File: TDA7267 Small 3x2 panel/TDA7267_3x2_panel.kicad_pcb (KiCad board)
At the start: 2 copper layers, 89 x 99 mm, 108 parts

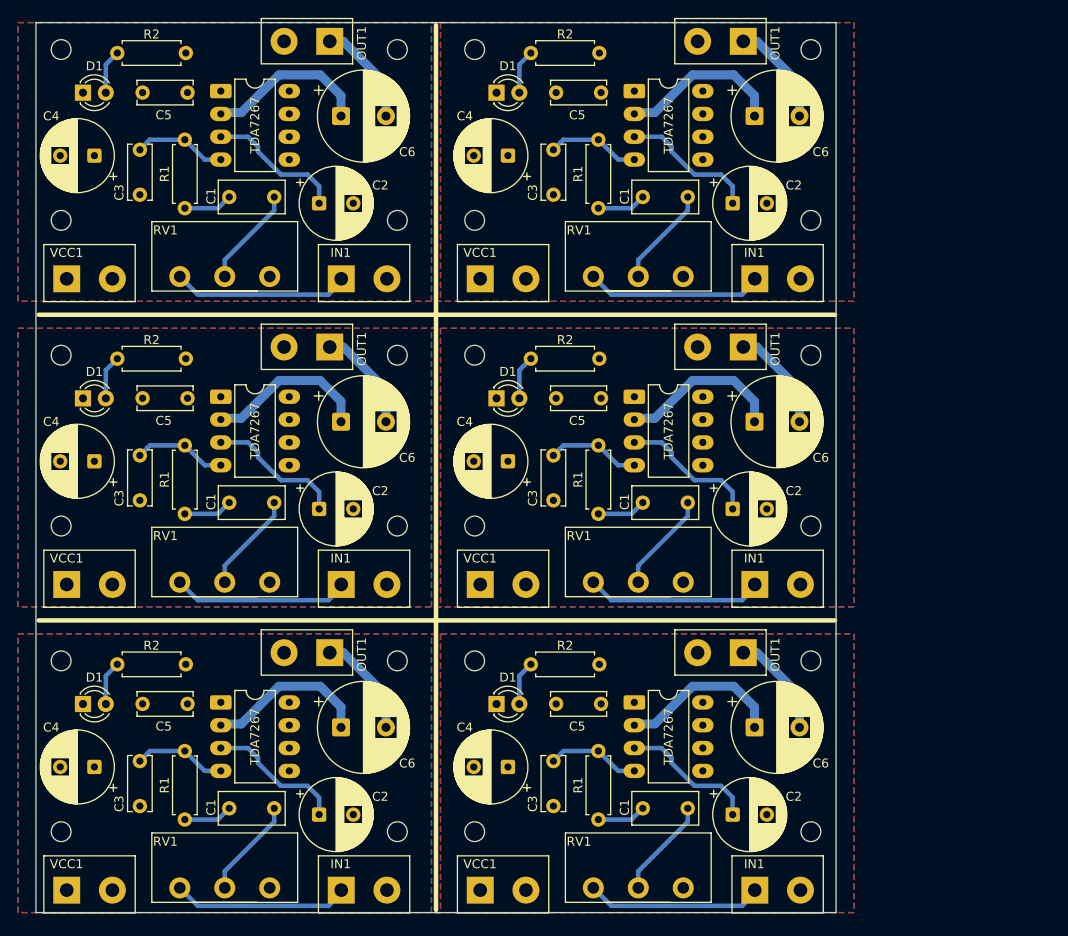
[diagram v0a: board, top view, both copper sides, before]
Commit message: Bottom GND plane
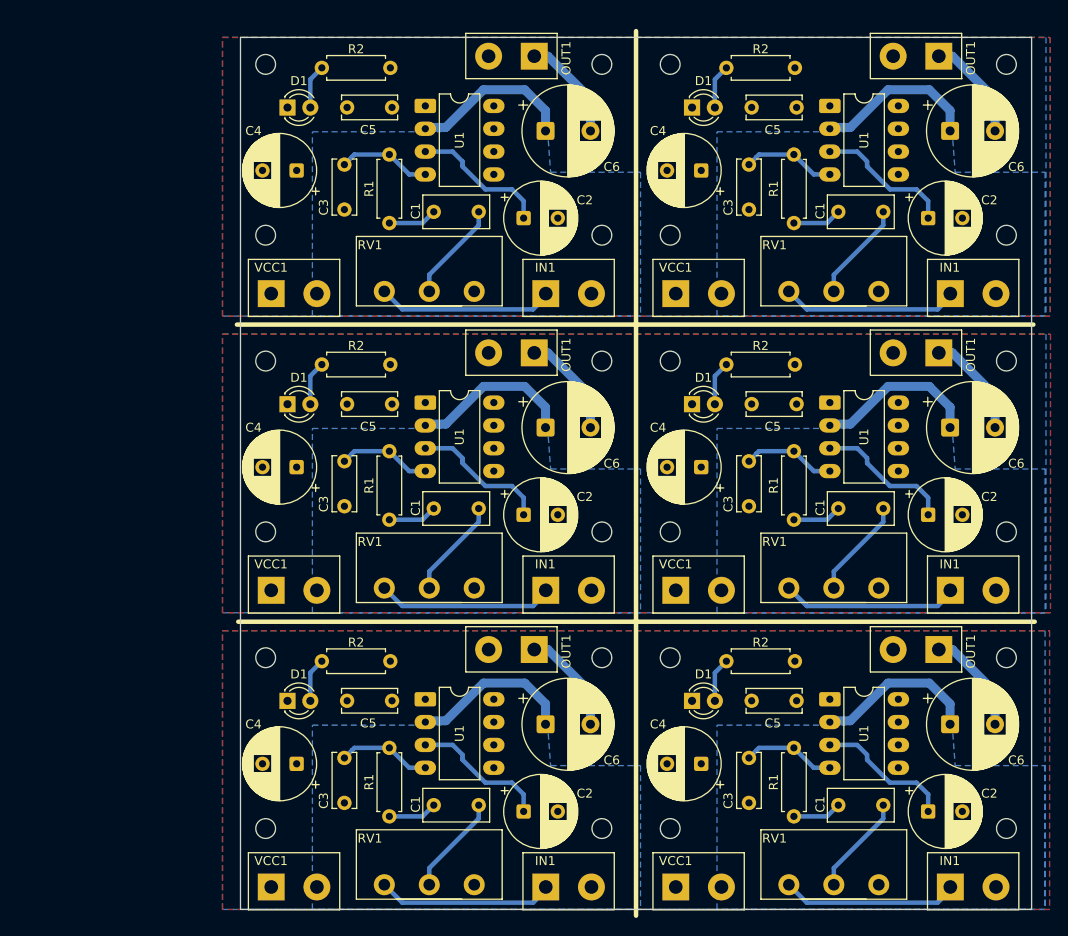
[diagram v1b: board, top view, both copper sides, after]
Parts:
- removed the C1 at (86.5, 127.4)
- removed the C1 at (86.5, 93.4)
- removed the C1 at (132.5, 127.4)
- removed the C1 at (132.5, 59.4)
- removed the C1 at (86.5, 59.4)
- removed the C1 at (132.5, 93.4)
- removed the C2 at (91.5, 60.1)
- removed the C2 at (137.5, 60.1)
- removed the C2 at (91.5, 94.1)
- removed the C2 at (137.5, 128.1)
- removed the C2 at (91.5, 128.1)
- removed the C2 at (137.5, 94.1)
- removed the C3 at (117.6, 59.1)
- removed the C3 at (117.6, 127.1)
- removed the C3 at (117.6, 93.1)
- removed the C3 at (71.6, 127.1)
- removed the C3 at (71.6, 93.1)
- removed the C3 at (71.6, 59.1)
- removed the C4 at (112.5, 54.8)
- removed the C4 at (112.5, 88.8)
- removed the C4 at (66.5, 88.8)
- removed the C4 at (66.5, 122.8)
- removed the C4 at (66.5, 54.8)
- removed the C4 at (112.5, 122.8)
- removed the C5 at (71.9, 47.8)
- removed the C5 at (117.9, 47.8)
- removed the C5 at (117.9, 115.8)
- removed the C5 at (117.9, 81.8)
- removed the C5 at (71.9, 115.8)
- removed the C5 at (71.9, 81.8)
- removed the C6 at (93.9, 50.4)
- removed the C6 at (93.9, 118.4)
- removed the C6 at (139.9, 118.4)
- removed the C6 at (139.9, 84.4)
- removed the C6 at (93.9, 84.4)
- removed the C6 at (139.9, 50.4)
- removed the D1 at (111.2, 115.8)
- removed the D1 at (65.2, 81.8)
- removed the D1 at (65.2, 47.8)
- removed the D1 at (65.2, 115.8)
- removed the D1 at (111.2, 47.8)
- removed the D1 at (111.2, 81.8)
- removed the H1 at (62.8, 77.0)
- removed the H1 at (108.8, 43.0)
- removed the H1 at (62.8, 43.0)
- removed the H1 at (108.8, 111.0)
- removed the H1 at (62.8, 111.0)
- removed the H1 at (108.8, 77.0)
- removed the H2 at (146.2, 111.0)
- removed the H2 at (100.2, 111.0)
- removed the H2 at (100.2, 77.0)
- removed the H2 at (146.2, 43.0)
- removed the H2 at (146.2, 77.0)
- removed the H2 at (100.2, 43.0)
- removed the H3 at (108.8, 62.0)
- removed the H3 at (108.8, 96.0)
- removed the H3 at (62.8, 96.0)
- removed the H3 at (108.8, 130.0)
- removed the H3 at (62.8, 62.0)
- removed the H3 at (62.8, 130.0)
- removed the H4 at (100.2, 62.0)
- removed the H4 at (146.2, 130.0)
- removed the H4 at (146.2, 96.0)
- removed the H4 at (146.2, 62.0)
- removed the H4 at (100.2, 130.0)
- removed the H4 at (100.2, 96.0)
- removed the IN1 at (94.0, 68.5)
- removed the IN1 at (140.0, 68.5)
- removed the IN1 at (94.0, 102.5)
- removed the IN1 at (94.0, 136.5)
- removed the IN1 at (140.0, 102.5)
- removed the IN1 at (140.0, 136.5)
- removed the OUT1 at (92.7, 42.1)
- removed the OUT1 at (138.7, 110.1)
- removed the OUT1 at (138.7, 42.1)
- removed the OUT1 at (138.7, 76.1)
- removed the OUT1 at (92.7, 76.1)
- removed the OUT1 at (92.7, 110.1)
- removed the R1 at (122.6, 60.6)
- removed the R1 at (122.6, 128.6)
- removed the R1 at (76.6, 128.6)
- removed the R1 at (122.6, 94.6)
- removed the R1 at (76.6, 60.6)
- removed the R1 at (76.6, 94.6)
- removed the R2 at (115.0, 43.4)
- removed the R2 at (69.0, 43.4)
- removed the R2 at (69.0, 111.4)
- removed the R2 at (69.0, 77.4)
- removed the R2 at (115.0, 77.4)
- removed the R2 at (115.0, 111.4)
- removed the RV1 at (76.0, 102.2)
- removed the RV1 at (76.0, 68.2)
- removed the RV1 at (76.0, 136.2)
- removed the RV1 at (122.0, 102.2)
- removed the RV1 at (122.0, 136.2)
- removed the RV1 at (122.0, 68.2)
- removed TDA7267 (x6): TDA7267, Package_DIP:DIP-8_W7.62mm_LongPads
- removed the VCC1 at (109.4, 68.5)
- removed the VCC1 at (63.4, 102.5)
- removed the VCC1 at (63.4, 136.5)
- removed the VCC1 at (63.4, 68.5)
- removed the VCC1 at (109.4, 102.5)
- removed the VCC1 at (109.4, 136.5)
- added C1: 1uF, Capacitor_THT:C_Rect_L7.2mm_W3.5mm_P5.00mm_FKS2_FKP2_MKS2_MKP2, F.Cu at (154.2, 94.0)
- added C1: 1uF, Capacitor_THT:C_Rect_L7.2mm_W3.5mm_P5.00mm_FKS2_FKP2_MKS2_MKP2, F.Cu at (109.2, 61.0)
- added C1: 1uF, Capacitor_THT:C_Rect_L7.2mm_W3.5mm_P5.00mm_FKS2_FKP2_MKS2_MKP2, F.Cu at (154.2, 61.0)
- added C1: 1uF, Capacitor_THT:C_Rect_L7.2mm_W3.5mm_P5.00mm_FKS2_FKP2_MKS2_MKP2, F.Cu at (109.2, 127.0)
- added C1: 1uF, Capacitor_THT:C_Rect_L7.2mm_W3.5mm_P5.00mm_FKS2_FKP2_MKS2_MKP2, F.Cu at (154.2, 127.0)
- added C1: 1uF, Capacitor_THT:C_Rect_L7.2mm_W3.5mm_P5.00mm_FKS2_FKP2_MKS2_MKP2, F.Cu at (109.2, 94.0)
- added C2: 47uF, Capacitor_THT:CP_Radial_D8.0mm_P3.80mm, F.Cu at (114.2, 61.8)
- added C2: 47uF, Capacitor_THT:CP_Radial_D8.0mm_P3.80mm, F.Cu at (114.2, 94.8)
- added C2: 47uF, Capacitor_THT:CP_Radial_D8.0mm_P3.80mm, F.Cu at (159.2, 127.8)
- added C2: 47uF, Capacitor_THT:CP_Radial_D8.0mm_P3.80mm, F.Cu at (159.2, 94.8)
- added C2: 47uF, Capacitor_THT:CP_Radial_D8.0mm_P3.80mm, F.Cu at (159.2, 61.8)
- added C2: 47uF, Capacitor_THT:CP_Radial_D8.0mm_P3.80mm, F.Cu at (114.2, 127.8)
- added C3: 470pF, Capacitor_THT:C_Disc_D6.0mm_W2.5mm_P5.00mm, F.Cu at (139.3, 60.8)
- added C3: 470pF, Capacitor_THT:C_Disc_D6.0mm_W2.5mm_P5.00mm, F.Cu at (94.3, 126.8)
- added C3: 470pF, Capacitor_THT:C_Disc_D6.0mm_W2.5mm_P5.00mm, F.Cu at (139.3, 93.8)
- added C3: 470pF, Capacitor_THT:C_Disc_D6.0mm_W2.5mm_P5.00mm, F.Cu at (139.3, 126.8)
- added C3: 470pF, Capacitor_THT:C_Disc_D6.0mm_W2.5mm_P5.00mm, F.Cu at (94.3, 60.8)
- added C3: 470pF, Capacitor_THT:C_Disc_D6.0mm_W2.5mm_P5.00mm, F.Cu at (94.3, 93.8)
- added C4: 100uF, Capacitor_THT:CP_Radial_D8.0mm_P3.80mm, F.Cu at (134.0, 56.5)
- added C4: 100uF, Capacitor_THT:CP_Radial_D8.0mm_P3.80mm, F.Cu at (89.0, 56.5)
- added C4: 100uF, Capacitor_THT:CP_Radial_D8.0mm_P3.80mm, F.Cu at (89.0, 122.5)
- added C4: 100uF, Capacitor_THT:CP_Radial_D8.0mm_P3.80mm, F.Cu at (89.0, 89.5)
- added C4: 100uF, Capacitor_THT:CP_Radial_D8.0mm_P3.80mm, F.Cu at (134.0, 89.5)
- added C4: 100uF, Capacitor_THT:CP_Radial_D8.0mm_P3.80mm, F.Cu at (134.0, 122.5)
- added C5: 100nF, Capacitor_THT:C_Disc_D6.0mm_W2.5mm_P5.00mm, F.Cu at (139.6, 49.4)
- added C5: 100nF, Capacitor_THT:C_Disc_D6.0mm_W2.5mm_P5.00mm, F.Cu at (139.6, 115.4)
- added C5: 100nF, Capacitor_THT:C_Disc_D6.0mm_W2.5mm_P5.00mm, F.Cu at (94.6, 82.4)
- added C5: 100nF, Capacitor_THT:C_Disc_D6.0mm_W2.5mm_P5.00mm, F.Cu at (139.6, 82.4)
- added C5: 100nF, Capacitor_THT:C_Disc_D6.0mm_W2.5mm_P5.00mm, F.Cu at (94.6, 115.4)
- added C5: 100nF, Capacitor_THT:C_Disc_D6.0mm_W2.5mm_P5.00mm, F.Cu at (94.6, 49.4)
- added C6: 1000uF, Capacitor_THT:CP_Radial_D10.0mm_P5.00mm, F.Cu at (116.7, 52.0)
- added C6: 1000uF, Capacitor_THT:CP_Radial_D10.0mm_P5.00mm, F.Cu at (161.7, 85.0)
- added C6: 1000uF, Capacitor_THT:CP_Radial_D10.0mm_P5.00mm, F.Cu at (116.7, 118.0)
- added C6: 1000uF, Capacitor_THT:CP_Radial_D10.0mm_P5.00mm, F.Cu at (161.7, 118.0)
- added C6: 1000uF, Capacitor_THT:CP_Radial_D10.0mm_P5.00mm, F.Cu at (116.7, 85.0)
- added C6: 1000uF, Capacitor_THT:CP_Radial_D10.0mm_P5.00mm, F.Cu at (161.7, 52.0)
- added D1: LED, LED_THT:LED_D3.0mm, F.Cu at (88.0, 82.5)
- added D1: LED, LED_THT:LED_D3.0mm, F.Cu at (133.0, 49.5)
- added D1: LED, LED_THT:LED_D3.0mm, F.Cu at (133.0, 115.5)
- added D1: LED, LED_THT:LED_D3.0mm, F.Cu at (133.0, 82.5)
- added D1: LED, LED_THT:LED_D3.0mm, F.Cu at (88.0, 115.5)
- added D1: LED, LED_THT:LED_D3.0mm, F.Cu at (88.0, 49.5)
- added H1: MountingHole, MountingHole:MountingHole_2.2mm_M2, F.Cu at (85.5, 77.7)
- added H1: MountingHole, MountingHole:MountingHole_2.2mm_M2, F.Cu at (130.6, 77.7)
- added H1: MountingHole, MountingHole:MountingHole_2.2mm_M2, F.Cu at (85.5, 44.6)
- added H1: MountingHole, MountingHole:MountingHole_2.2mm_M2, F.Cu at (130.6, 110.7)
- added H1: MountingHole, MountingHole:MountingHole_2.2mm_M2, F.Cu at (130.6, 44.6)
- added H1: MountingHole, MountingHole:MountingHole_2.2mm_M2, F.Cu at (85.5, 110.7)
- added H2: MountingHole, MountingHole:MountingHole_2.2mm_M2, F.Cu at (167.9, 44.6)
- added H2: MountingHole, MountingHole:MountingHole_2.2mm_M2, F.Cu at (167.9, 77.7)
- added H2: MountingHole, MountingHole:MountingHole_2.2mm_M2, F.Cu at (123.0, 77.7)
- added H2: MountingHole, MountingHole:MountingHole_2.2mm_M2, F.Cu at (123.0, 110.7)
- added H2: MountingHole, MountingHole:MountingHole_2.2mm_M2, F.Cu at (167.9, 110.7)
- added H2: MountingHole, MountingHole:MountingHole_2.2mm_M2, F.Cu at (123.0, 44.6)
- added H3: MountingHole, MountingHole:MountingHole_2.2mm_M2, F.Cu at (85.5, 96.7)
- added H3: MountingHole, MountingHole:MountingHole_2.2mm_M2, F.Cu at (85.5, 63.6)
- added H3: MountingHole, MountingHole:MountingHole_2.2mm_M2, F.Cu at (130.6, 129.7)
- added H3: MountingHole, MountingHole:MountingHole_2.2mm_M2, F.Cu at (130.6, 63.6)
- added H3: MountingHole, MountingHole:MountingHole_2.2mm_M2, F.Cu at (85.5, 129.7)
- added H3: MountingHole, MountingHole:MountingHole_2.2mm_M2, F.Cu at (130.6, 96.7)
- added H4: MountingHole, MountingHole:MountingHole_2.2mm_M2, F.Cu at (123.0, 96.7)
- added H4: MountingHole, MountingHole:MountingHole_2.2mm_M2, F.Cu at (123.0, 63.6)
- added H4: MountingHole, MountingHole:MountingHole_2.2mm_M2, F.Cu at (167.9, 129.7)
- added H4: MountingHole, MountingHole:MountingHole_2.2mm_M2, F.Cu at (123.0, 129.7)
- added H4: MountingHole, MountingHole:MountingHole_2.2mm_M2, F.Cu at (167.9, 96.7)
- added H4: MountingHole, MountingHole:MountingHole_2.2mm_M2, F.Cu at (167.9, 63.6)
- added IN1: Conn_01x02_Pin, TerminalBlock:TerminalBlock_bornier-2_P5.08mm, F.Cu at (161.7, 70.2)
- added IN1: Conn_01x02_Pin, TerminalBlock:TerminalBlock_bornier-2_P5.08mm, F.Cu at (116.7, 70.2)
- added IN1: Conn_01x02_Pin, TerminalBlock:TerminalBlock_bornier-2_P5.08mm, F.Cu at (116.7, 103.2)
- added IN1: Conn_01x02_Pin, TerminalBlock:TerminalBlock_bornier-2_P5.08mm, F.Cu at (161.7, 136.2)
- added IN1: Conn_01x02_Pin, TerminalBlock:TerminalBlock_bornier-2_P5.08mm, F.Cu at (116.7, 136.2)
- added IN1: Conn_01x02_Pin, TerminalBlock:TerminalBlock_bornier-2_P5.08mm, F.Cu at (161.7, 103.2)
- added OUT1: Conn_01x02_Pin, TerminalBlock:TerminalBlock_bornier-2_P5.08mm, F.Cu at (115.4, 76.7)
- added OUT1: Conn_01x02_Pin, TerminalBlock:TerminalBlock_bornier-2_P5.08mm, F.Cu at (160.4, 76.7)
- added OUT1: Conn_01x02_Pin, TerminalBlock:TerminalBlock_bornier-2_P5.08mm, F.Cu at (160.4, 43.7)
- added OUT1: Conn_01x02_Pin, TerminalBlock:TerminalBlock_bornier-2_P5.08mm, F.Cu at (115.4, 43.7)
- added OUT1: Conn_01x02_Pin, TerminalBlock:TerminalBlock_bornier-2_P5.08mm, F.Cu at (160.4, 109.7)
- added OUT1: Conn_01x02_Pin, TerminalBlock:TerminalBlock_bornier-2_P5.08mm, F.Cu at (115.4, 109.7)
- added R1: 1K, Resistor_THT:R_Axial_DIN0207_L6.3mm_D2.5mm_P7.62mm_Horizontal, F.Cu at (144.3, 128.3)
- added R1: 1K, Resistor_THT:R_Axial_DIN0207_L6.3mm_D2.5mm_P7.62mm_Horizontal, F.Cu at (99.3, 128.3)
- added R1: 1K, Resistor_THT:R_Axial_DIN0207_L6.3mm_D2.5mm_P7.62mm_Horizontal, F.Cu at (144.3, 95.3)
- added R1: 1K, Resistor_THT:R_Axial_DIN0207_L6.3mm_D2.5mm_P7.62mm_Horizontal, F.Cu at (99.3, 62.3)
- added R1: 1K, Resistor_THT:R_Axial_DIN0207_L6.3mm_D2.5mm_P7.62mm_Horizontal, F.Cu at (144.3, 62.3)
- added R1: 1K, Resistor_THT:R_Axial_DIN0207_L6.3mm_D2.5mm_P7.62mm_Horizontal, F.Cu at (99.3, 95.3)
- added R2: 1K, Resistor_THT:R_Axial_DIN0207_L6.3mm_D2.5mm_P7.62mm_Horizontal, F.Cu at (91.8, 78.0)
- added R2: 1K, Resistor_THT:R_Axial_DIN0207_L6.3mm_D2.5mm_P7.62mm_Horizontal, F.Cu at (91.8, 45.0)
- added R2: 1K, Resistor_THT:R_Axial_DIN0207_L6.3mm_D2.5mm_P7.62mm_Horizontal, F.Cu at (136.8, 111.0)
- added R2: 1K, Resistor_THT:R_Axial_DIN0207_L6.3mm_D2.5mm_P7.62mm_Horizontal, F.Cu at (136.8, 78.0)
- added R2: 1K, Resistor_THT:R_Axial_DIN0207_L6.3mm_D2.5mm_P7.62mm_Horizontal, F.Cu at (91.8, 111.0)
- added R2: 1K, Resistor_THT:R_Axial_DIN0207_L6.3mm_D2.5mm_P7.62mm_Horizontal, F.Cu at (136.8, 45.0)
- added RV1: R_Potentiometer, Potentiometer_THT:Potentiometer_Piher_T-16H_Single_Horizontal, F.Cu at (143.8, 102.9)
- added RV1: R_Potentiometer, Potentiometer_THT:Potentiometer_Piher_T-16H_Single_Horizontal, F.Cu at (98.8, 69.9)
- added RV1: R_Potentiometer, Potentiometer_THT:Potentiometer_Piher_T-16H_Single_Horizontal, F.Cu at (98.8, 135.9)
- added RV1: R_Potentiometer, Potentiometer_THT:Potentiometer_Piher_T-16H_Single_Horizontal, F.Cu at (143.8, 69.9)
- added RV1: R_Potentiometer, Potentiometer_THT:Potentiometer_Piher_T-16H_Single_Horizontal, F.Cu at (98.8, 102.9)
- added RV1: R_Potentiometer, Potentiometer_THT:Potentiometer_Piher_T-16H_Single_Horizontal, F.Cu at (143.8, 135.9)
- added U1: TDA7267, Package_DIP:DIP-8_W7.62mm_LongPads, F.Cu at (103.3, 82.3)
- added U1: TDA7267, Package_DIP:DIP-8_W7.62mm_LongPads, F.Cu at (103.3, 49.3)
- added U1: TDA7267, Package_DIP:DIP-8_W7.62mm_LongPads, F.Cu at (148.3, 82.3)
- added U1: TDA7267, Package_DIP:DIP-8_W7.62mm_LongPads, F.Cu at (148.3, 49.3)
- added U1: TDA7267, Package_DIP:DIP-8_W7.62mm_LongPads, F.Cu at (148.3, 115.3)
- added U1: TDA7267, Package_DIP:DIP-8_W7.62mm_LongPads, F.Cu at (103.3, 115.3)
- added VCC1: Conn_01x02_Pin, TerminalBlock:TerminalBlock_bornier-2_P5.08mm, F.Cu at (86.2, 136.2)
- added VCC1: Conn_01x02_Pin, TerminalBlock:TerminalBlock_bornier-2_P5.08mm, F.Cu at (131.2, 103.2)
- added VCC1: Conn_01x02_Pin, TerminalBlock:TerminalBlock_bornier-2_P5.08mm, F.Cu at (131.2, 136.2)
- added VCC1: Conn_01x02_Pin, TerminalBlock:TerminalBlock_bornier-2_P5.08mm, F.Cu at (86.2, 103.2)
- added VCC1: Conn_01x02_Pin, TerminalBlock:TerminalBlock_bornier-2_P5.08mm, F.Cu at (86.2, 70.2)
- added VCC1: Conn_01x02_Pin, TerminalBlock:TerminalBlock_bornier-2_P5.08mm, F.Cu at (131.2, 70.2)
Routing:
- added copper zone on B.Cu, net /VCC
- added copper zone on B.Cu, net GND
- removed copper zone on B.Cu, net Net-(U1-V+)
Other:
- board size 89 x 99 mm -> 88 x 97 mm
- board text added: "TDA7267 2.5W Amplifier. 5 to 15V DC supply."
- board text removed: "TDA7267 2W Amplifier. 5 to 15V DC supply."

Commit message: Tweaks
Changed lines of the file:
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@@
 				(thickness 0.035)
 			)
-			(layer "dielectric 1"
+			(layer "dielectric 2"
 				(type "core")
 				(thickness 1.51)
@@
 		(hatch edge 0.5)
 		(connect_pads yes
-			(clearance 0.5)
+			(clearance 0.3)
 		)
 		(min_thickness 0.25)
@@
 		(hatch edge 0.5)
 		(connect_pads yes
-			(clearance 0.5)
+			(clearance 0.3)
 		)
 		(min_thickness 0.25)
@@
 		(hatch edge 0.5)
 		(connect_pads yes
-			(clearance 0.5)
+			(clearance 0.3)
 		)
 		(min_thickness 0.25)
@@
 		(priority 1)
 		(connect_pads yes
-			(clearance 0.5)
+			(clearance 0.3)
 		)
 		(min_thickness 0.25)
@@
 		(priority 1)
 		(connect_pads yes
-			(clearance 0.5)
+			(clearance 0.3)
 		)
 		(min_thickness 0.25)
@@
 			(pts
 				(xy 90.75 72.65) (xy 90.75 52.15) (xy 105 52.15) (xy 110 47.4) (xy 114.5 47.4) (xy 116.75 49.9)
-				(xy 117.25 56.65) (xy 127.25 56.65) (xy 127.25 72.65)
+				(xy 117.25 56.65) (xy 126.75 56.65) (xy 126.75 72.65)
 			)
 		)
@@
 		(hatch edge 0.5)
 		(connect_pads yes
-			(clearance 0.5)
+			(clearance 0.3)
 		)
 		(min_thickness 0.25)
@@
 		(hatch edge 0.5)
 		(connect_pads yes
-			(clearance 0.5)
+			(clearance 0.3)
 		)
 		(min_thickness 0.25)
@@
 		(priority 1)
 		(connect_pads yes
-			(clearance 0.5)
+			(clearance 0.3)
 		)
 		(min_thickness 0.25)
@@
 			(pts
 				(xy 90.75 105.65) (xy 90.75 85.15) (xy 105 85.15) (xy 110 80.4) (xy 114.5 80.4) (xy 116.75 82.9)
-				(xy 117.25 89.65) (xy 127.25 89.65) (xy 127.25 105.65)
+				(xy 117.25 89.65) (xy 126.75 89.65) (xy 126.75 105.65)
 			)
 		)
@@
 		(priority 1)
 		(connect_pads yes
-			(clearance 0.5)
+			(clearance 0.3)
 		)
 		(min_thickness 0.25)
@@
 			(pts
 				(xy 90.75 138.65) (xy 90.75 118.15) (xy 105 118.15) (xy 110 113.4) (xy 114.5 113.4) (xy 116.75 115.9)
-				(xy 117.25 122.65) (xy 127.25 122.65) (xy 127.25 138.65)
+				(xy 117.25 122.65) (xy 126.75 122.65) (xy 126.75 138.65)
 			)
 		)
@@
 		(priority 1)
 		(connect_pads yes
-			(clearance 0.5)
+			(clearance 0.3)
 		)
 		(min_thickness 0.25)
@@
 		(hatch edge 0.5)
 		(connect_pads yes
-			(clearance 0.5)
+			(clearance 0.3)
 		)
 		(min_thickness 0.25)
@@
 		(priority 1)
 		(connect_pads yes
-			(clearance 0.5)
+			(clearance 0.3)
 		)
 		(min_thickness 0.25)
